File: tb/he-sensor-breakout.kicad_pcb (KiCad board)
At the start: 2 copper layers, 19.1 x 17.8 mm, 28 parts, among them J1 Conn_01x01_Pin, J10 Conn_01x01_Pin, J11 Conn_01x01_Pin, J12 Conn_01x01_Pin, J13 Conn_01x01_Pin, J14 Conn_01x01_Pin, J2 Conn_01x01_Pin, J3 Conn_01x01_Pin, J4 Conn_01x01_Pin, J5 Conn_01x01_Pin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

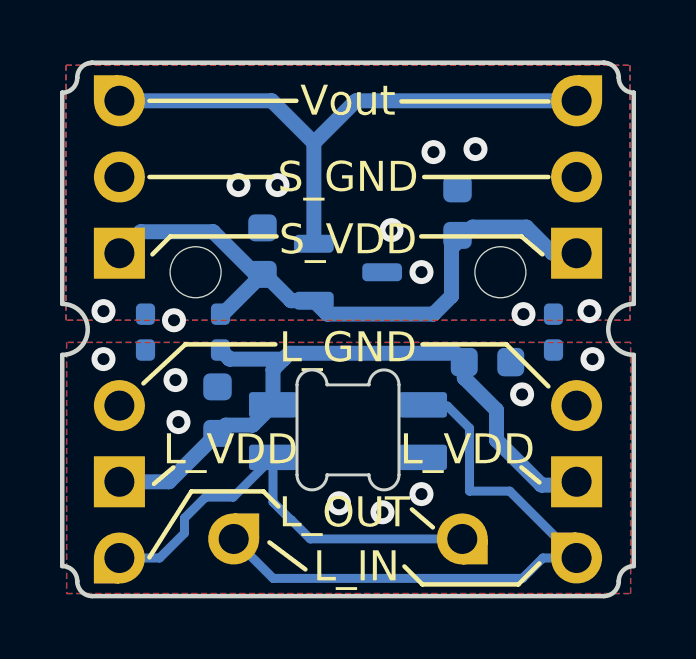
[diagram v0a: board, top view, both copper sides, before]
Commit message: make the 1u taller by a tiny bit
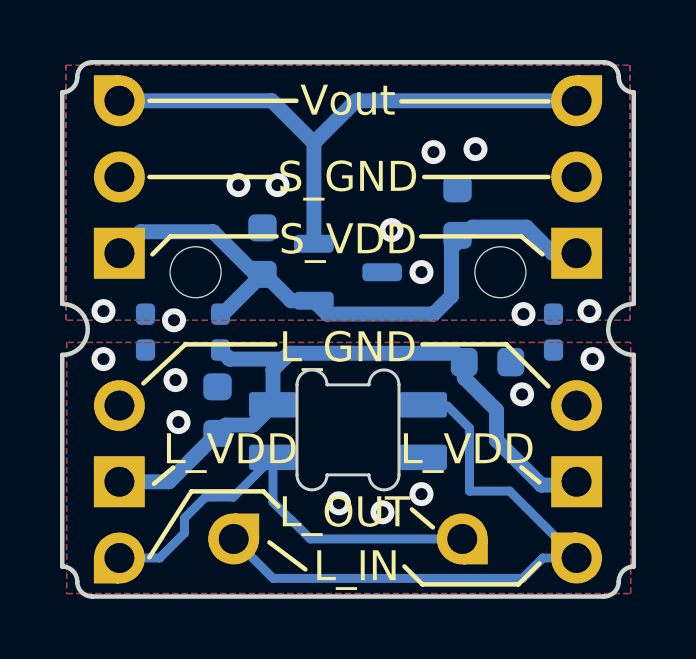
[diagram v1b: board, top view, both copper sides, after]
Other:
- outline, holes or cut-outs redrawn
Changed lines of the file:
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@@
   (gr_arc (start 118.745026 103.6) (mid 116.745 101.6) (end 118.745026 99.6)
     (stroke (width 0.15) (type default)) (layer "Dwgs.User"))
-  (gr_arc (start 100.195 93.21) (mid 100.048553 93.563553) (end 99.695 93.71)
+  (gr_arc (start 100.195 93.195) (mid 100.048553 93.548553) (end 99.695 93.695)
     (stroke (width 0.15) (type default)) (layer "Edge.Cuts"))
   (gr_arc (start 118.745 102.45) (mid 117.895 101.6) (end 118.745 100.75)
     (stroke (width 0.15) (type default)) (layer "Edge.Cuts"))
-  (gr_line (start 99.695 93.71) (end 99.695 100.75)
+  (gr_line (start 99.695 93.695) (end 99.695 100.75)
     (stroke (width 0.15) (type default)) (layer "Edge.Cuts"))
-  (gr_line (start 117.745 110.49) (end 100.695 110.49)
+  (gr_line (start 117.745 110.505) (end 100.695 110.505)
     (stroke (width 0.15) (type default)) (layer "Edge.Cuts"))
-  (gr_line (start 118.745 102.45) (end 118.745 109.49)
+  (gr_line (start 118.745 102.45) (end 118.745 109.505)
     (stroke (width 0.15) (type default)) (layer "Edge.Cuts"))
-  (gr_line (start 118.745 93.71) (end 118.745 100.75)
+  (gr_line (start 118.745 93.695) (end 118.745 100.75)
     (stroke (width 0.15) (type default)) (layer "Edge.Cuts"))
-  (gr_line (start 99.695 102.45) (end 99.695 109.49)
+  (gr_line (start 99.695 102.45) (end 99.695 109.505)
     (stroke (width 0.15) (type default)) (layer "Edge.Cuts"))
   (gr_arc (start 99.695 100.75) (mid 100.545 101.6) (end 99.695 102.45)
     (stroke (width 0.15) (type default)) (layer "Edge.Cuts"))
-  (gr_line (start 100.695 92.71) (end 117.745 92.71)
+  (gr_line (start 100.695 92.695) (end 117.745 92.695)
     (stroke (width 0.15) (type default)) (layer "Edge.Cuts"))
-  (gr_arc (start 100.195 93.21) (mid 100.341447 92.856447) (end 100.695 92.71)
+  (gr_arc (start 100.195 93.195) (mid 100.341447 92.841447) (end 100.695 92.695)
     (stroke (width 0.15) (type default)) (layer "Edge.Cuts"))
-  (gr_arc (start 118.245 109.99) (mid 118.098612 110.343612) (end 117.745 110.49)
+  (gr_arc (start 118.245 110.005) (mid 118.098612 110.358612) (end 117.745 110.505)
     (stroke (width 0.15) (type default)) (layer "Edge.Cuts"))
-  (gr_arc (start 117.745 92.71) (mid 118.098553 92.856447) (end 118.245 93.21)
+  (gr_arc (start 117.745 92.695) (mid 118.098553 92.841447) (end 118.245 93.195)
     (stroke (width 0.15) (type default)) (layer "Edge.Cuts"))
-  (gr_arc (start 99.695 109.49) (mid 100.048553 109.636447) (end 100.195 109.99)
+  (gr_arc (start 99.695 109.505) (mid 100.048553 109.651447) (end 100.195 110.005)
     (stroke (width 0.15) (type default)) (layer "Edge.Cuts"))
-  (gr_arc (start 118.745 93.71) (mid 118.391447 93.563553) (end 118.245 93.21)
+  (gr_arc (start 118.745 93.695) (mid 118.391447 93.548553) (end 118.245 93.195)
     (stroke (width 0.15) (type default)) (layer "Edge.Cuts"))
-  (gr_arc (start 100.695 110.49) (mid 100.341447 110.343553) (end 100.195 109.99)
+  (gr_arc (start 100.695 110.505) (mid 100.341447 110.358553) (end 100.195 110.005)
     (stroke (width 0.15) (type default)) (layer "Edge.Cuts"))
-  (gr_arc (start 118.245 109.99) (mid 118.391505 109.636505) (end 118.745 109.49)
+  (gr_arc (start 118.245 110.005) (mid 118.391505 109.651505) (end 118.745 109.505)
     (stroke (width 0.15) (type default)) (layer "Edge.Cuts"))
   (gr_text "S_GND\n" (at 109.2 95.5) (layer "B.SilkS")
